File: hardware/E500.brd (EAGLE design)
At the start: 38.1 x 31.9 mm, 27 parts, among them SW1 SPST_TACT-KMR2, U11 915MHz, U5 ATMEGA328P-MU, U8 MCP1703CB, X1 16 MHz

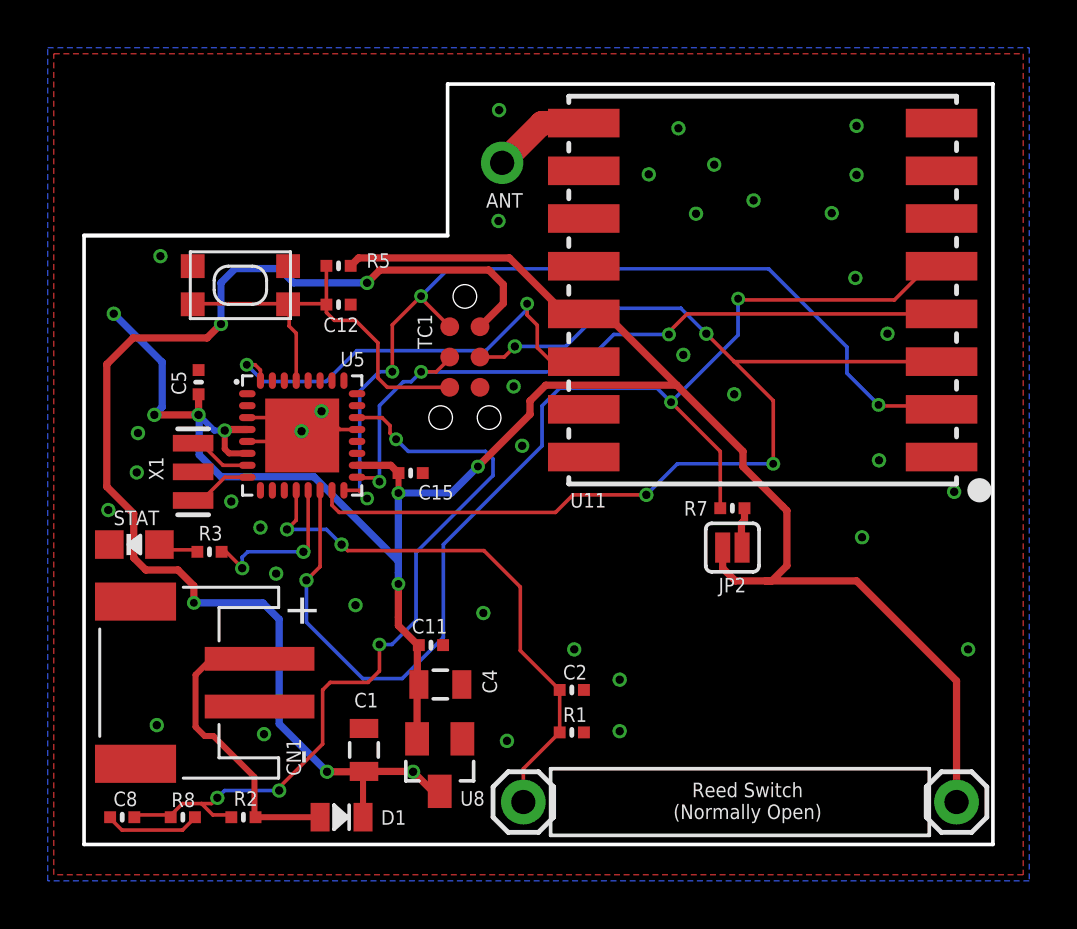
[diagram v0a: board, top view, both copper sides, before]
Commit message: v2.2 - minor update
- removed solder jumper from SS pin
- added bottom silkscreen for node id
- DRU mask limit to 14mil for covering via with solder mask
- very minor trace adjustment
- functionally same as previous
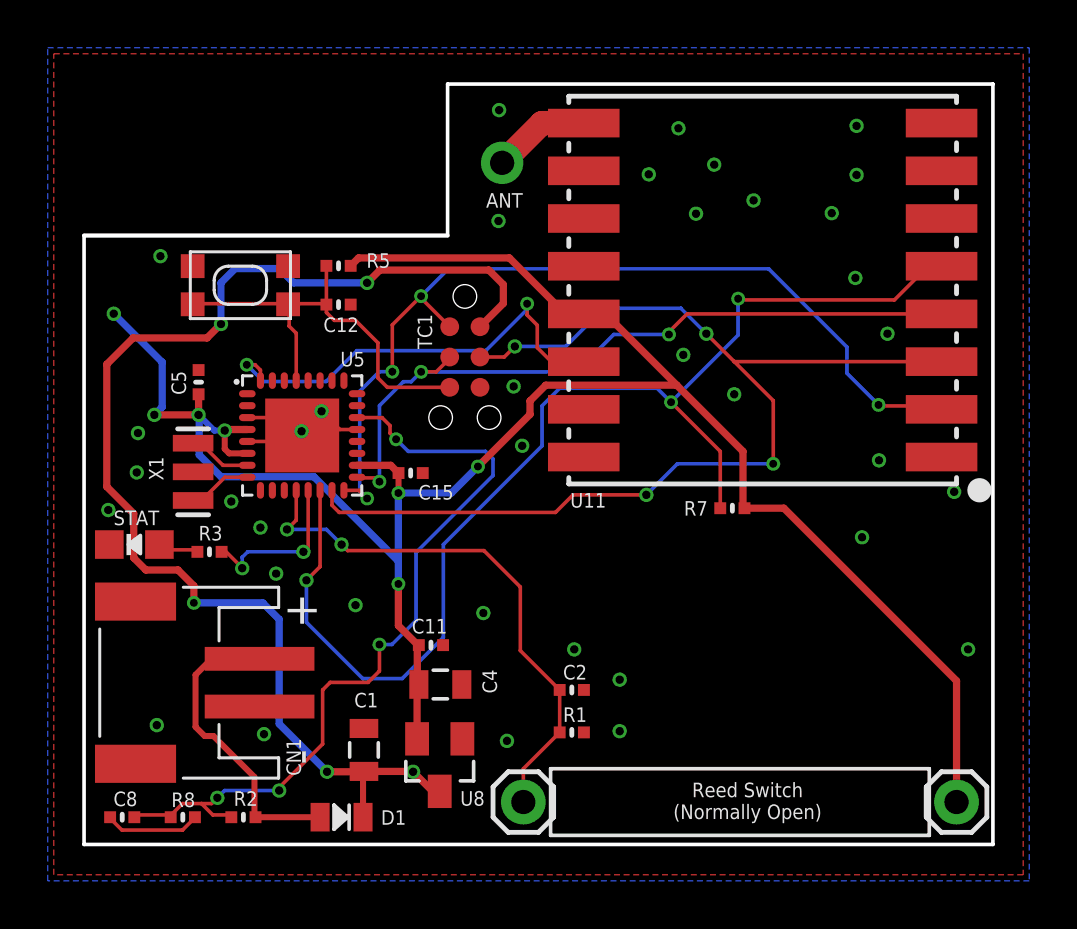
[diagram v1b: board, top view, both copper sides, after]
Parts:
- removed JP2: JUMPER-SMT_2_NC_PASTE_SILK, SparkFun-Jumpers:SMT-JUMPER_2_NC_PASTE_SILK
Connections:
- removed net N$11: JP2.1, R7.2
- net VCC: now also R7.2; no longer JP2.2
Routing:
- net VCC: track 95.7 -> 90.6 mm
- net N$11: track 1.71 -> 0.00 mm
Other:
- board text added: "v2.2 | October 2019"
- board text removed: "v2.1 | July 2019"
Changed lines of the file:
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@@
 <?xml version="1.0" encoding="utf-8"?>
 <!DOCTYPE eagle SYSTEM "eagle.dtd">
-<eagle version="9.4.1">
+<eagle version="9.5.1">
 <drawing>
 <settings>
@@
 <text x="37.084" y="75.3364" size="1.016" layer="122" font="vector" ratio="16" rot="MR90" align="center-right">Elemental</text>
 <text x="0.508" y="49.9364" size="0.6096" layer="122" font="vector" rot="MR90" align="bottom-center">Designed by Akram Ali</text>
-<text x="35.7632" y="75.3364" size="0.6096" layer="122" font="vector" rot="MR270" align="center-left">v2.1 | July 2019</text>
+<text x="35.7632" y="75.3364" size="0.6096" layer="122" font="vector" rot="MR270" align="center-left">v2.2 | October 2019</text>
 <text x="34.6202" y="75.3618" size="0.8128" layer="122" font="vector" ratio="12" rot="MR90" align="center-right">elemental-platform.com</text>
 <wire x1="0" y1="69.85" x2="15.24" y2="69.85" width="0.1778" layer="20"/>
@@
 <text x="27.813" y="45.3898" size="0.6096" layer="121" font="vector" align="bottom-center">Reed Switch
 (Normally Open)</text>
+<polygon width="0.3048" layer="122">
+<vertex x="1.651" y="44.958"/>
+<vertex x="16.764" y="44.958"/>
+<vertex x="16.764" y="55.499"/>
+<vertex x="1.651" y="55.499"/>
+</polygon>
 </plain>
 <attributes>
@@
 </class>
 </classes>
-<designrules name="oshpark-2layer">
+<designrules name="oshpark-2layer *">
 <description language="en">&lt;b&gt;OSH Park Design Rules&lt;/b&gt;
 &lt;p&gt;
@@
 <param name="mlMinCreamFrame" value="0mil"/>
 <param name="mlMaxCreamFrame" value="0mil"/>
-<param name="mlViaStopLimit" value="0mil"/>
+<param name="mlViaStopLimit" value="14mil"/>
 <param name="srRoundness" value="0"/>
 <param name="srMinRoundness" value="0mil"/>
@@
 <attribute name="NAME" x="4.8006" y="57.0675" size="0.6096" layer="121" font="vector"/>
 </element>
-<element name="JP2" library="SparkFun-Jumpers" library_urn="urn:adsk.eagle:library:528" package="SMT-JUMPER_2_NC_PASTE_SILK" package3d_urn="urn:adsk.eagle:package:39282/1" value="JUMPER-SMT_2_NC_PASTE_SILK" x="27.178" y="56.769" smashed="yes" rot="R180">
-<attribute name="NAME" x="27.178" y="55.499" size="0.6096" layer="121" font="vector" rot="R180" align="bottom-center"/>
-</element>
 <element name="D1" library="SCHOTTKY_0805" package="0805" value="" x="10.795" y="45.466" smashed="yes">
 <attribute name="NAME" x="12.446" y="45.1485" size="0.6096" layer="121" font="vector"/>
@@
 <wire x1="13.97" y1="52.54625" x2="14.0335" y2="52.6796" width="0.254" layer="1"/>
 <wire x1="13.97" y1="51.1175" x2="14.0352" y2="51.0286" width="0.1524" layer="1"/>
-<wire x1="13.17625" y1="55.245" x2="13.17625" y2="55.72125" width="0.3048" layer="16"/>
 <wire x1="13.17625" y1="56.1975" x2="13.17625" y2="59.055" width="0.3048" layer="16"/>
-<wire x1="13.17625" y1="53.49875" x2="13.17625" y2="53.848" width="0.3048" layer="1"/>
-<wire x1="13.17625" y1="53.848" x2="13.17625" y2="55.245" width="0.3048" layer="1"/>
+<wire x1="13.17625" y1="53.49875" x2="13.17625" y2="55.245" width="0.3048" layer="1"/>
 <wire x1="13.97" y1="52.705" x2="13.17625" y2="53.49875" width="0.3048" layer="1"/>
 <wire x1="13.97" y1="52.705" x2="14.0335" y2="52.6796" width="0.1524" layer="1"/>
@@
 <wire x1="20.948" y1="66.564" x2="20.79625" y2="66.675" width="0.1524" layer="1"/>
 <wire x1="21.9075" y1="66.51625" x2="24.84755" y2="63.5762" width="0.3048" layer="1"/>
-<wire x1="24.84755" y1="63.5762" x2="27.6225" y2="60.80125" width="0.3048" layer="1"/>
+<wire x1="27.6225" y1="60.80125" x2="24.84755" y2="63.5762" width="0.3048" layer="1"/>
 <wire x1="20.955" y1="66.51625" x2="21.9075" y2="66.51625" width="0.3048" layer="1"/>
 <wire x1="20.955" y1="66.51625" x2="20.948" y2="66.564" width="0.1524" layer="1"/>
@@
 <wire x1="6.844" y1="61.718" x2="5.93800625" y2="61.718" width="0.3048" layer="1"/>
 <wire x1="5.93800625" y1="61.718" x2="5.896815625" y2="61.676809375" width="0.254" layer="1"/>
-<wire x1="27.6225" y1="60.80125" x2="27.6225" y2="60.1599" width="0.3048" layer="1"/>
-<wire x1="27.6225" y1="60.1599" x2="29.2862" y2="58.4962" width="0.3048" layer="1"/>
 <via x="1.2446" y="66.5734" extent="1-16" drill="0.35"/>
 <wire x1="1.2446" y1="66.5734" x2="3.2766" y2="64.5414" width="0.3048" layer="16"/>
@@
 <wire x1="20.79625" y1="66.675" x2="20.066" y2="66.675" width="0.3048" layer="1"/>
 <wire x1="20.066" y1="66.675" x2="17.8308" y2="68.9102" width="0.3048" layer="1"/>
-<contactref element="JP2" pad="2"/>
-<wire x1="26.7716" y1="56.769" x2="26.7716" y2="55.9054" width="0.3048" layer="1"/>
-<wire x1="26.7716" y1="55.9054" x2="27.305" y2="55.372" width="0.3048" layer="1"/>
 <contactref element="J2" pad="1"/>
-<wire x1="13.17625" y1="55.72125" x2="13.17625" y2="56.1975" width="0.3048" layer="16"/>
-<wire x1="27.305" y1="55.372" x2="28.575" y2="55.372" width="0.3048" layer="1"/>
-<wire x1="28.575" y1="55.372" x2="28.829" y2="55.372" width="0.3048" layer="1"/>
-<wire x1="28.829" y1="55.372" x2="29.464" y2="56.007" width="0.3048" layer="1"/>
-<wire x1="29.464" y1="56.007" x2="29.464" y2="58.3184" width="0.3048" layer="1"/>
-<wire x1="29.464" y1="58.3184" x2="29.2862" y2="58.4962" width="0.3048" layer="1"/>
-<wire x1="36.576" y1="46.101" x2="36.576" y2="51.181" width="0.3048" layer="1"/>
-<wire x1="32.385" y1="55.372" x2="28.575" y2="55.372" width="0.3048" layer="1"/>
-<wire x1="36.576" y1="51.181" x2="32.385" y2="55.372" width="0.3048" layer="1"/>
+<wire x1="13.17625" y1="55.245" x2="13.17625" y2="56.1975" width="0.3048" layer="16"/>
+<wire x1="36.576" y1="51.181" x2="36.576" y2="46.101" width="0.3048" layer="1"/>
+<contactref element="R7" pad="2"/>
+<wire x1="27.686" y1="58.42" x2="27.6225" y2="58.4835" width="0.3048" layer="1"/>
+<wire x1="27.6225" y1="58.4835" x2="27.6225" y2="60.80125" width="0.3048" layer="1"/>
+<wire x1="27.686" y1="58.42" x2="29.337" y2="58.42" width="0.3048" layer="1"/>
+<wire x1="29.337" y1="58.42" x2="36.576" y2="51.181" width="0.3048" layer="1"/>
 </signal>
 <signal name="SCL">
@@
 <wire x1="3.175" y1="56.8325" x2="3.1582" y2="56.896" width="0.1524" layer="1"/>
 </signal>
-<signal name="N$11">
-<contactref element="R7" pad="2"/>
-<contactref element="JP2" pad="1"/>
-<wire x1="27.686" y1="58.42" x2="27.686" y2="57.912" width="0.3048" layer="1"/>
-<wire x1="27.686" y1="57.912" x2="27.559" y2="57.785" width="0.3048" layer="1"/>
-<wire x1="27.559" y1="57.785" x2="27.559" y2="56.7944" width="0.3048" layer="1"/>
-<wire x1="27.559" y1="56.7944" x2="27.5844" y2="56.769" width="0.3048" layer="1"/>
-</signal>
 </signals>
